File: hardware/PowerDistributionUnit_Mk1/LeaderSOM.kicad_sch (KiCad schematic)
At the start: 14 parts, among them J10 Logic Analyzer, J11 Logic Analyzer, J12 Logic Analyzer, U1 LeaderSOM

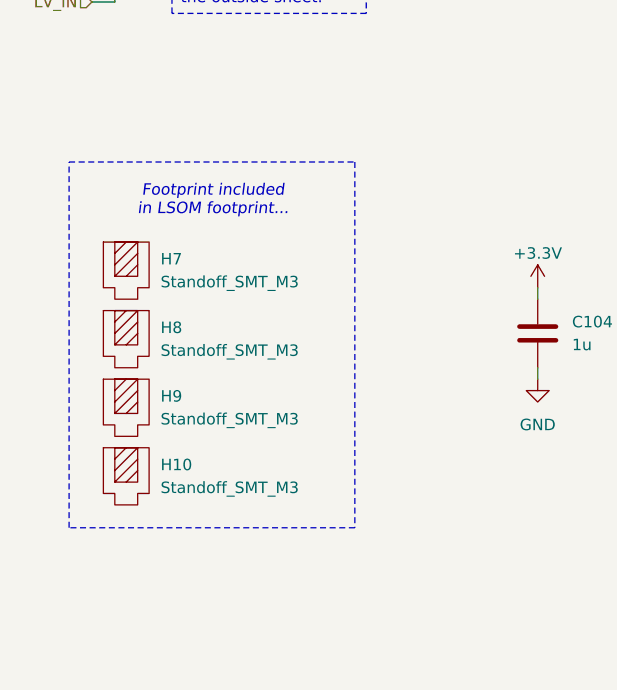
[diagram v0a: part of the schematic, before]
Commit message: update schematic documentation, clean up, update titleblocks
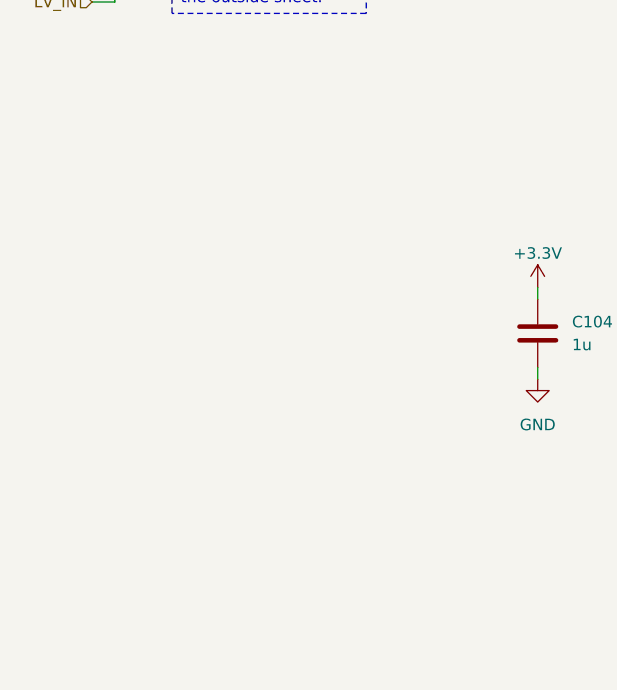
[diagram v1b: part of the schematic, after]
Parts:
- removed H10, H7, H8, H9: Standoff_SMT_M3, PowerDistributionUnitLib:78614040360, symbol PowerDistributionUnitLib:Standoff_SMT_78614040360
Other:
- note removed: "Footprint included in LSOM footprint..."

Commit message: update all symbols with LCSC P/N
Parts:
- C104, C105, C6: LCSC P/N (none) -> C15849
- D36: LCSC P/N (none) -> C5628891
- R24: LCSC P/N (none) -> C22808
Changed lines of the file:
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@@
+			)
+		)
+		(property "LCSC P/N" "C15849"
+			(at 99.06 66.04 0)
+			(effects
+				(font
+					(size 1.27 1.27)
+				)
+				(hide yes)
 			)
 		)
@@
 			)
 		)
+		(property "LCSC P/N" "C22808"
+			(at 55.88 138.43 0)
+			(effects
+				(font
+					(size 1.27 1.27)
+				)
+				(hide yes)
+			)
+		)
 		(pin "1"
 		)
@@
 			)
 		)
+		(property "LCSC P/N" "C5628891"
+			(at 50.8 127 0)
+			(effects
+				(font
+					(size 1.27 1.27)
+				)
+				(hide yes)
+			)
+		)
 		(pin "4"
 		)
@@
 			)
 		)
+		(property "LCSC P/N" "C15849"
+			(at 99.06 43.18 0)
+			(effects
+				(font
+					(size 1.27 1.27)
+				)
+				(hide yes)
+			)
+		)
 		(pin "1"
 		)
@@
 			(at 87.63 66.04 0)
 			(effects
+				(font
+					(size 1.27 1.27)
+				)
+				(hide yes)
+			)
+		)
+		(property "LCSC P/N" "C15849"
+			(at 87.63 66.04 0)
+			(effects
